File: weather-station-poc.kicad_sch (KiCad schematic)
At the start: 14 parts

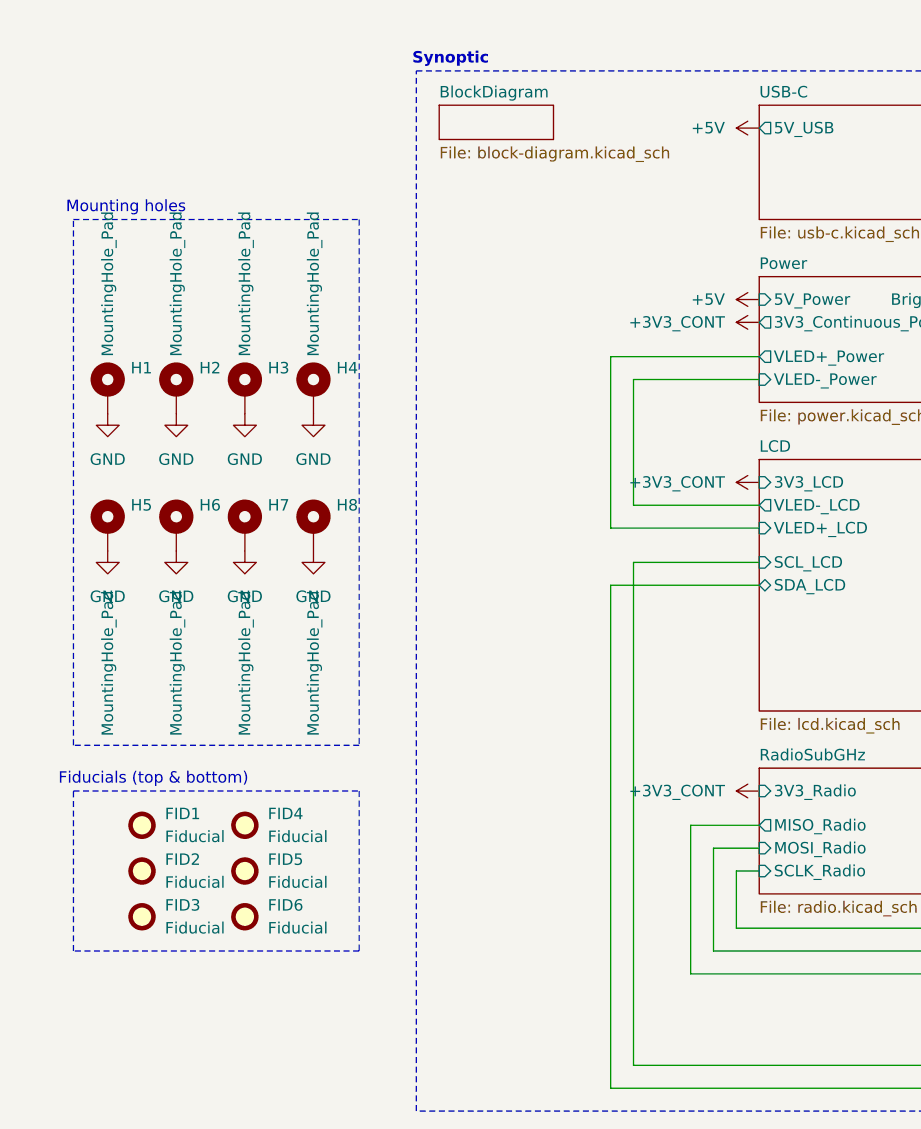
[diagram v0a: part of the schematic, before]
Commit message: Update schematic to Kicad 10
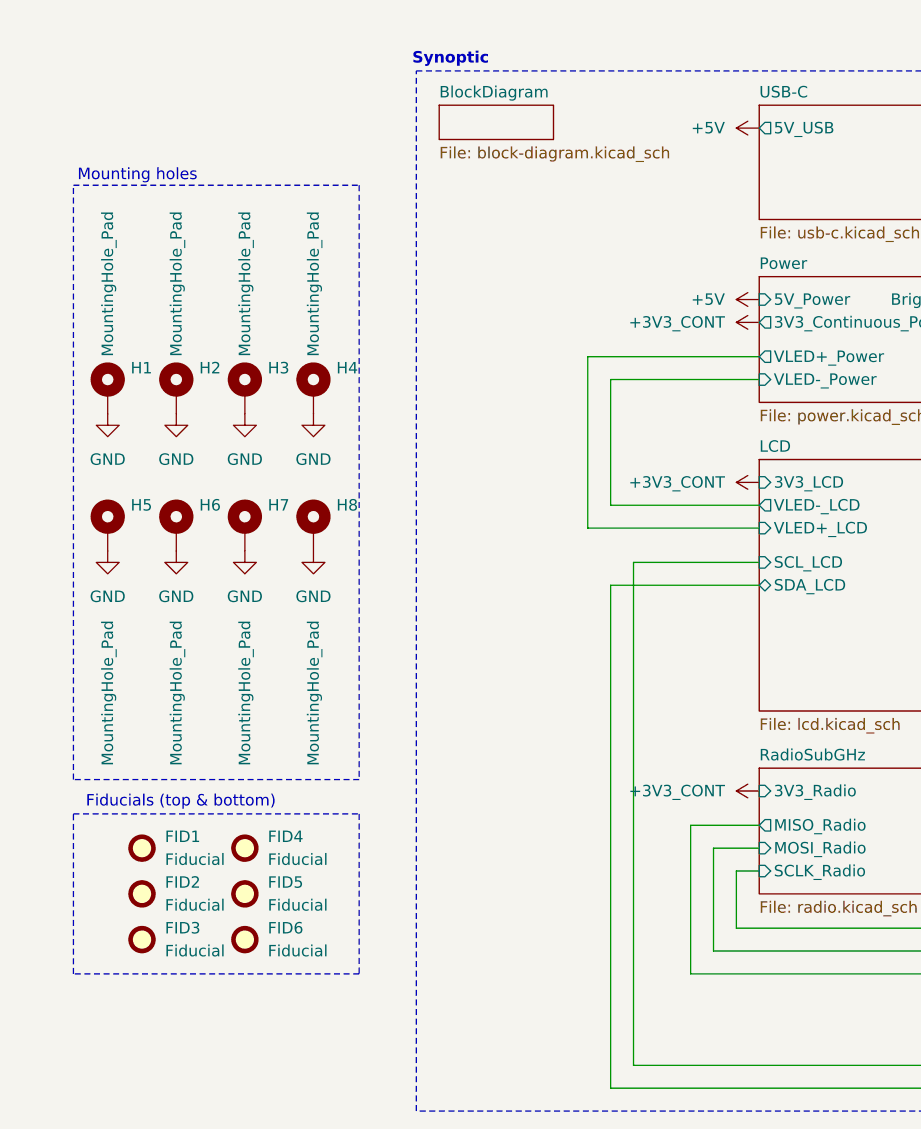
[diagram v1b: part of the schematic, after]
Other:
- moved on the sheet: FID1, FID2, FID3, FID4, FID5, FID6

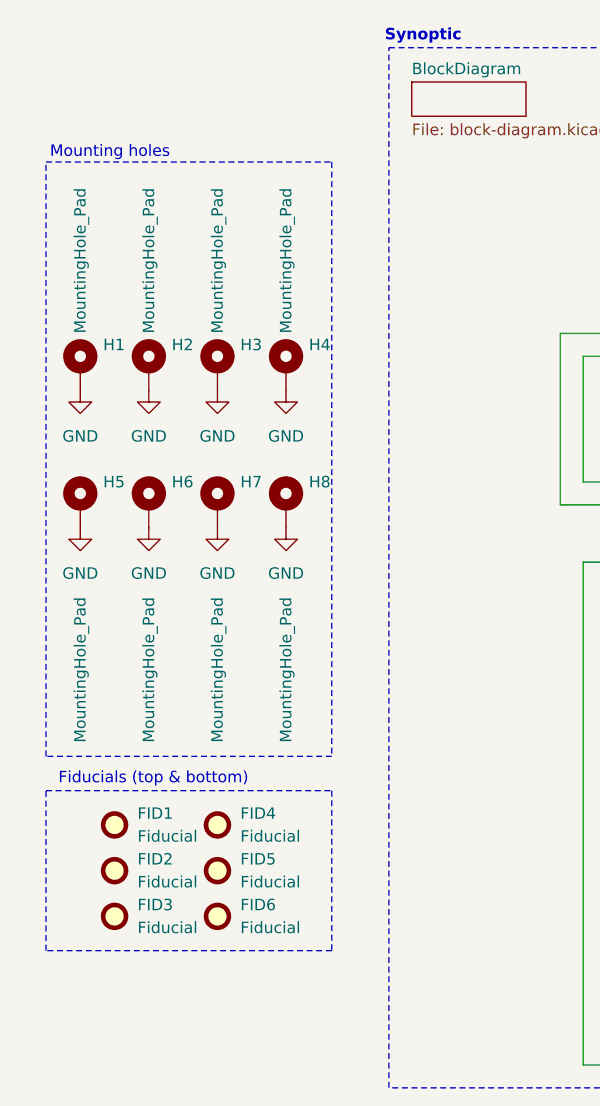
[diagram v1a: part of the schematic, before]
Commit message: Add tests points with 5015 footprint for practicity
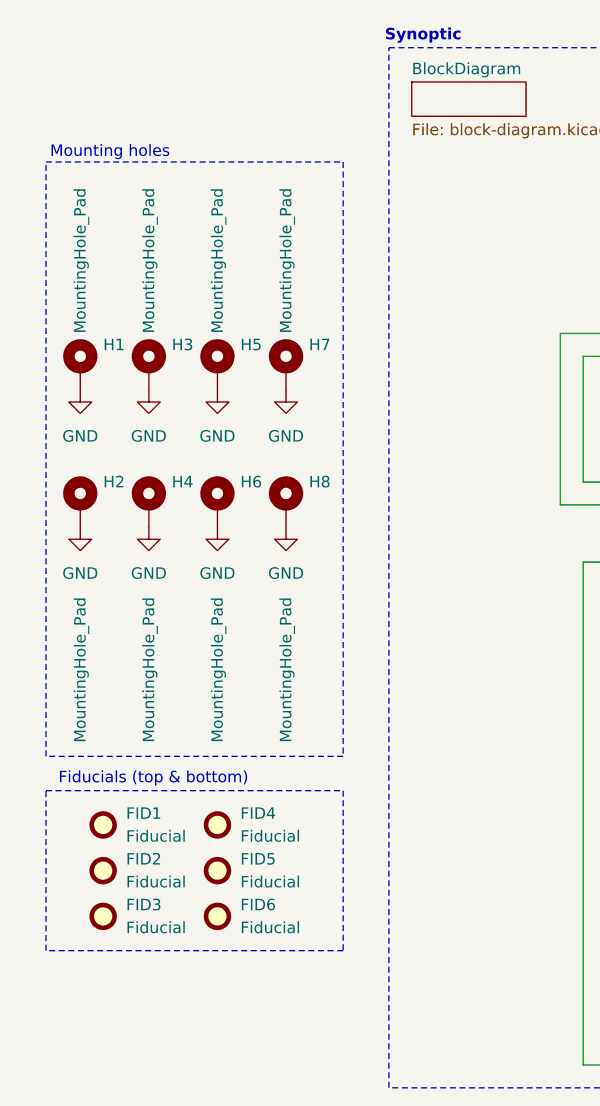
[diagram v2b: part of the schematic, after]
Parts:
- renumbered H5 to H2, H2 to H3, H6 to H4, H3 to H5, H7 to H6, H4 to H7
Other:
- moved on the sheet: FID1, FID2, FID3
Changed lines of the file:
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@@
 	(rectangle
 		(start 19.05 118.11)
-		(end 50.8 135.89)
+		(end 52.07 135.89)
 		(stroke
 			(width 0)
@@
 	(rectangle
 		(start 19.05 48.26)
-		(end 50.8 114.3)
+		(end 52.07 114.3)
 		(stroke
 			(width 0)
@@
 		(dnp no)
 		(fields_autoplaced yes)
-		(property "Reference" "#PWR0124"
+		(property "Reference" "#PWR02"
 			(at 22.86 95.25 0)
 			(hide yes)
@@
 			(project "weather-station-poc"
 				(path "/38eb53bb-294e-46e4-ad59-fd355ca373b9"
-					(reference "#PWR0124")
+					(reference "#PWR02")
 					(unit 1)
 				)
@@
 		(dnp no)
 		(fields_autoplaced yes)
-		(property "Reference" "#PWR0122"
+		(property "Reference" "#PWR05"
 			(at 38.1 80.01 0)
 			(hide yes)
@@
 			(project "weather-station-poc"
 				(path "/38eb53bb-294e-46e4-ad59-fd355ca373b9"
-					(reference "#PWR0122")
+					(reference "#PWR05")
 					(unit 1)
 				)
@@
 		(in_pos_files yes)
 		(dnp no)
-		(property "Reference" "H3"
+		(property "Reference" "H5"
 			(at 40.64 68.5799 0)
 			(show_name no)
@@
 			(project "weather-station-poc"
 				(path "/38eb53bb-294e-46e4-ad59-fd355ca373b9"
-					(reference "H3")
+					(reference "H5")
 					(unit 1)
 				)
@@
 		(in_pos_files yes)
 		(dnp no)
-		(property "Reference" "#PWR02"
+		(property "Reference" "#PWR015"
 			(at 222.25 41.91 0)
 			(hide yes)
@@
 			(project "weather-station-poc"
 				(path "/38eb53bb-294e-46e4-ad59-fd355ca373b9"
-					(reference "#PWR02")
+					(reference "#PWR015")
 					(unit 1)
 				)
@@
 		(in_pos_files yes)
 		(dnp no)
-		(property "Reference" "H5"
+		(property "Reference" "H2"
 			(at 25.4 83.8199 0)
 			(show_name no)
@@
 			(project "weather-station-poc"
 				(path "/38eb53bb-294e-46e4-ad59-fd355ca373b9"
-					(reference "H5")
+					(reference "H2")
 					(unit 1)
 				)
@@
 		(dnp no)
 		(fields_autoplaced yes)
-		(property "Reference" "#PWR0121"
+		(property "Reference" "#PWR03"
 			(at 30.48 80.01 0)
 			(hide yes)
@@
 			(project "weather-station-poc"
 				(path "/38eb53bb-294e-46e4-ad59-fd355ca373b9"
-					(reference "#PWR0121")
+					(reference "#PWR03")
 					(unit 1)
 				)
@@
 		(in_pos_files yes)
 		(dnp no)
-		(property "Reference" "#PWR06"
+		(property "Reference" "#PWR016"
 			(at 222.25 85.09 0)
 			(hide yes)
@@
 			(project "weather-station-poc"
 				(path "/38eb53bb-294e-46e4-ad59-fd355ca373b9"
-					(reference "#PWR06")
+					(reference "#PWR016")
 					(unit 1)
 				)
@@
 		(in_pos_files yes)
 		(dnp no)
-		(property "Reference" "#PWR07"
+		(property "Reference" "#PWR017"
 			(at 222.25 102.87 0)
 			(hide yes)
@@
 			(project "weather-station-poc"
 				(path "/38eb53bb-294e-46e4-ad59-fd355ca373b9"
-					(reference "#PWR07")
+					(reference "#PWR017")
 					(unit 1)
 				)
@@
 		(in_pos_files yes)
 		(dnp no)
-		(property "Reference" "H7"
+		(property "Reference" "H6"
 			(at 40.64 83.8199 0)
 			(show_name no)
@@
 			(project "weather-station-poc"
 				(path "/38eb53bb-294e-46e4-ad59-fd355ca373b9"
-					(reference "H7")
+					(reference "H6")
 					(unit 1)
 				)
@@
 	(symbol
 		(lib_id "Mechanical:Fiducial")
-		(at 26.67 121.92 0)
+		(at 25.4 121.92 0)
 		(unit 1)
 		(body_style 1)
@@
 		(fields_autoplaced yes)
 		(property "Reference" "FID1"
-			(at 29.21 120.6499 0)
+			(at 27.94 120.6499 0)
 			(show_name no)
 			(do_not_autoplace no)
@@
 		)
 		(property "Value" "Fiducial"
-			(at 29.21 123.1899 0)
+			(at 27.94 123.1899 0)
 			(show_name no)
 			(do_not_autoplace no)
@@
 		)
 		(property "Footprint" "Fiducial:Fiducial_1mm_Mask2mm"
-			(at 26.67 121.92 0)
+			(at 25.4 121.92 0)
 			(hide yes)
 			(show_name no)
@@
 		)
 		(property "Datasheet" ""
-			(at 26.67 121.92 0)
+			(at 25.4 121.92 0)
 			(hide yes)
 			(show_name no)
@@
 		)
 		(property "Description" "Fiducial Marker"
-			(at 26.67 121.92 0)
+			(at 25.4 121.92 0)
 			(hide yes)
 			(show_name no)
@@
 		(dnp no)
 		(fields_autoplaced yes)
-		(property "Reference" "#PWR0120"
+		(property "Reference" "#PWR01"
 			(at 22.86 80.01 0)
 			(hide yes)
@@
 			(project "weather-station-poc"
 				(path "/38eb53bb-294e-46e4-ad59-fd355ca373b9"
-					(reference "#PWR0120")
+					(reference "#PWR01")
 					(unit 1)
 				)
@@
 	(symbol
 		(lib_id "Mechanical:Fiducial")
-		(at 26.67 132.08 0)
+		(at 25.4 132.08 0)
 		(unit 1)
 		(body_style 1)
@@
 		(fields_autoplaced yes)
 		(property "Reference" "FID3"
-			(at 29.21 130.8099 0)
+			(at 27.94 130.8099 0)
 			(show_name no)
 			(do_not_autoplace no)
@@
 		)
 		(property "Value" "Fiducial"
-			(at 29.21 133.3499 0)
+			(at 27.94 133.3499 0)
 			(show_name no)
 			(do_not_autoplace no)
@@
 		)
 		(property "Footprint" "Fiducial:Fiducial_1mm_Mask2mm"
-			(at 26.67 132.08 0)
+			(at 25.4 132.08 0)
 			(hide yes)
 			(show_name no)
@@
 		)
 		(property "Datasheet" ""
-			(at 26.67 132.08 0)
+			(at 25.4 132.08 0)
 			(hide yes)
 			(show_name no)
@@
 		)
 		(property "Description" "Fiducial Marker"
-			(at 26.67 132.08 0)
+			(at 25.4 132.08 0)
 			(hide yes)
 			(show_name no)
@@
 		(in_pos_files yes)
 		(dnp no)
-		(property "Reference" "H2"
+		(property "Reference" "H3"
 			(at 33.02 68.5799 0)
 			(show_name no)
@@
 			(project "weather-station-poc"
 				(path "/38eb53bb-294e-46e4-ad59-fd355ca373b9"
-					(reference "H2")
+					(reference "H3")
 					(unit 1)
 				)
@@
 		(dnp no)
 		(fields_autoplaced yes)
-		(property "Reference" "#PWR0126"
+		(property "Reference" "#PWR08"
 			(at 45.72 95.25 0)
 			(hide yes)
@@
 			(project "weather-station-poc"
 				(path "/38eb53bb-294e-46e4-ad59-fd355ca373b9"
-					(reference "#PWR0126")
+					(reference "#PWR08")
 					(unit 1)
 				)
@@
 		(dnp no)
 		(fields_autoplaced yes)
-		(property "Reference" "#PWR0123"
+		(property "Reference" "#PWR07"
 			(at 45.72 80.01 0)
 			(hide yes)
@@
 			(project "weather-station-poc"
 				(path "/38eb53bb-294e-46e4-ad59-fd355ca373b9"
-					(reference "#PWR0123")
+					(reference "#PWR07")
 					(unit 1)
 				)
@@
 		(dnp no)
 		(fields_autoplaced yes)
-		(property "Reference" "#PWR03"
+		(property "Reference" "#PWR010"
 			(at 99.06 60.96 0)
 			(hide yes)
@@
 			(project "weather-station-poc"
 				(path "/38eb53bb-294e-46e4-ad59-fd355ca373b9"
-					(reference "#PWR03")
+					(reference "#PWR010")
 					(unit 1)
 				)
@@
 		(in_pos_files yes)
 		(dnp no)
-		(property "Reference" "#PWR04"
+		(property "Reference" "#PWR011"
 			(at 99.06 63.5 0)
 			(hide yes)
@@
 			(project "weather-station-poc"
 				(path "/38eb53bb-294e-46e4-ad59-fd355ca373b9"
-					(reference "#PWR04")
+					(reference "#PWR011")
 					(unit 1)
 				)
@@
 		(dnp no)
 		(fields_autoplaced yes)
-		(property "Reference" "#PWR0127"
+		(property "Reference" "#PWR06"
 			(at 38.1 95.25 0)
 			(hide yes)
@@
 			(project "weather-station-poc"
 				(path "/38eb53bb-294e-46e4-ad59-fd355ca373b9"
-					(reference "#PWR0127")
+					(reference "#PWR06")
 					(unit 1)
 				)
@@
 		(in_pos_files yes)
 		(dnp no)
-		(property "Reference" "H6"
+		(property "Reference" "H4"
 			(at 33.02 83.8199 0)
 			(show_name no)
@@
 			(project "weather-station-poc"
 				(path "/38eb53bb-294e-46e4-ad59-fd355ca373b9"
-					(reference "H6")
+					(reference "H4")
 					(unit 1)
 				)
@@
 		(dnp no)
 		(fields_autoplaced yes)
-		(property "Reference" "#PWR0125"
+		(property "Reference" "#PWR04"
 			(at 30.48 95.25 0)
 			(hide yes)
@@
 			(project "weather-station-poc"
 				(path "/38eb53bb-294e-46e4-ad59-fd355ca373b9"
-					(reference "#PWR0125")
+					(reference "#PWR04")
 					(unit 1)
 				)
@@
 		(in_pos_files yes)
 		(dnp no)
-		(property "Reference" "H4"
+		(property "Reference" "H7"
 			(at 48.26 68.5799 0)
 			(show_name no)
@@
 			(project "weather-station-poc"
 				(path "/38eb53bb-294e-46e4-ad59-fd355ca373b9"
-					(reference "H4")
+					(reference "H7")
 					(unit 1)
 				)
@@
 		(dnp no)
 		(fields_autoplaced yes)
-		(property "Reference" "#PWR01"
+		(property "Reference" "#PWR09"
 			(at 99.06 41.91 0)
 			(hide yes)
@@
 			(project "weather-station-poc"
 				(path "/38eb53bb-294e-46e4-ad59-fd355ca373b9"
-					(reference "#PWR01")
+					(reference "#PWR09")
 					(unit 1)
 				)
@@
 		(in_pos_files yes)
 		(dnp no)
-		(property "Reference" "#PWR09"
+		(property "Reference" "#PWR014"
 			(at 148.59 139.7 0)
 			(hide yes)
@@
 			(project "weather-station-poc"
 				(path "/38eb53bb-294e-46e4-ad59-fd355ca373b9"
-					(reference "#PWR09")
+					(reference "#PWR014")
 					(unit 1)
 				)
@@
 	(symbol
 		(lib_id "Mechanical:Fiducial")
-		(at 26.67 127 0)
+		(at 25.4 127 0)
 		(unit 1)
 		(body_style 1)
@@
 		(fields_autoplaced yes)
 		(property "Reference" "FID2"
-			(at 29.21 125.7299 0)
+			(at 27.94 125.7299 0)
 			(show_name no)
 			(do_not_autoplace no)
@@
 		)
 		(property "Value" "Fiducial"
-			(at 29.21 128.2699 0)
+			(at 27.94 128.2699 0)
 			(show_name no)
 			(do_not_autoplace no)
@@
 		)
 		(property "Footprint" "Fiducial:Fiducial_1mm_Mask2mm"
-			(at 26.67 127 0)
+			(at 25.4 127 0)
 			(hide yes)
 			(show_name no)
@@
 		)
 		(property "Datasheet" ""
-			(at 26.67 127 0)
+			(at 25.4 127 0)
 			(hide yes)
 			(show_name no)
@@
 		)
 		(property "Description" "Fiducial Marker"
-			(at 26.67 127 0)
+			(at 25.4 127 0)
 			(hide yes)
 			(show_name no)
@@
 		(in_pos_files yes)
 		(dnp no)
-		(property "Reference" "#PWR05"
+		(property "Reference" "#PWR012"
 			(at 99.06 81.28 0)
 			(hide yes)
@@
 			(project "weather-station-poc"
 				(path "/38eb53bb-294e-46e4-ad59-fd355ca373b9"
-					(reference "#PWR05")
+					(reference "#PWR012")
 					(unit 1)
 				)
@@
 		(in_pos_files yes)
 		(dnp no)
-		(property "Reference" "#PWR08"
+		(property "Reference" "#PWR013"
 			(at 99.06 115.57 0)
 			(hide yes)
@@
 			(project "weather-station-poc"
 				(path "/38eb53bb-294e-46e4-ad59-fd355ca373b9"
-					(reference "#PWR08")
+					(reference "#PWR013")
 					(unit 1)
 				)
